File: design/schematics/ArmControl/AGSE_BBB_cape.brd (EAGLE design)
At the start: 71.8 x 54.6 mm, 50 parts, among them Q1 PFET-FQP27P06, Q2 PFET-FQP27P06, Q3 NFET-FQP30N06L, Q4 NFET-FQP30N06L, Q5 PFET-FQP27P06, Q6 PFET-FQP27P06, Q7 NFET-FQP30N06L, Q8 NFET-FQP30N06L, U1 V_REG_LD1085D2

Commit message: updated schematic to move tx/rx connection from UART1 to UART5
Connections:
- net BBB_RX: now also U$1.38; no longer U$1.68, U$1.72
- net BBB_TX: now also U$1.37; no longer U$1.67, U$1.70
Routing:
- net BBB_RX: track 37.2 -> 9.72 mm
- net BBB_TX: track 29.4 -> 23.6 mm
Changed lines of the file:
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@@
 <contactref element="R16" pad="2"/>
 <contactref element="R15" pad="1"/>
-<contactref element="U$1" pad="68"/>
-<contactref element="U$1" pad="72"/>
-<wire x1="38.989" y1="4.699" x2="54.102" y2="19.812" width="0.3048" layer="16"/>
 <wire x1="54.102" y1="19.812" x2="58.293" y2="19.812" width="0.3048" layer="16"/>
 <via x="58.293" y="19.812" extent="1-16" drill="0.6" shape="square"/>
 <wire x1="58.293" y1="19.812" x2="58.293" y2="22.545" width="0.4064" layer="1"/>
 <wire x1="58.293" y1="22.545" x2="61.087" y2="22.545" width="0.4064" layer="1"/>
-<wire x1="38.989" y1="4.699" x2="37.719" y2="5.969" width="0.4064" layer="1"/>
-<wire x1="37.719" y1="5.969" x2="35.433" y2="5.969" width="0.4064" layer="1"/>
-<wire x1="35.433" y1="5.969" x2="34.163" y2="4.699" width="0.4064" layer="1"/>
-<wire x1="34.163" y1="4.699" x2="33.909" y2="4.699" width="0.4064" layer="1"/>
+<contactref element="U$1" pad="38"/>
+<wire x1="58.293" y1="22.545" x2="54.229" y2="52.959" width="0" layer="19" extent="1-1"/>
 </signal>
 <signal name="BBB_TX">
 <contactref element="R14" pad="2"/>
-<contactref element="U$1" pad="67"/>
-<contactref element="U$1" pad="70"/>
-<wire x1="33.909" y1="2.159" x2="36.449" y2="4.699" width="0.4064" layer="1"/>
-<wire x1="36.449" y1="4.699" x2="37.973" y2="6.223" width="0.3048" layer="16"/>
 <wire x1="37.973" y1="6.223" x2="39.497" y2="6.223" width="0.3048" layer="16"/>
 <wire x1="39.497" y1="6.223" x2="51.435" y2="18.161" width="0.3048" layer="16"/>
@@
 <wire x1="51.435" y1="21.209" x2="50.485" y2="20.259" width="0.4064" layer="1"/>
 <wire x1="50.485" y1="20.259" x2="50.485" y2="19.431" width="0.4064" layer="1"/>
+<contactref element="U$1" pad="37"/>
+<wire x1="51.435" y1="21.209" x2="54.229" y2="50.419" width="0" layer="19" extent="1-1"/>
 </signal>
 <signal name="BBB_EQEP2A">

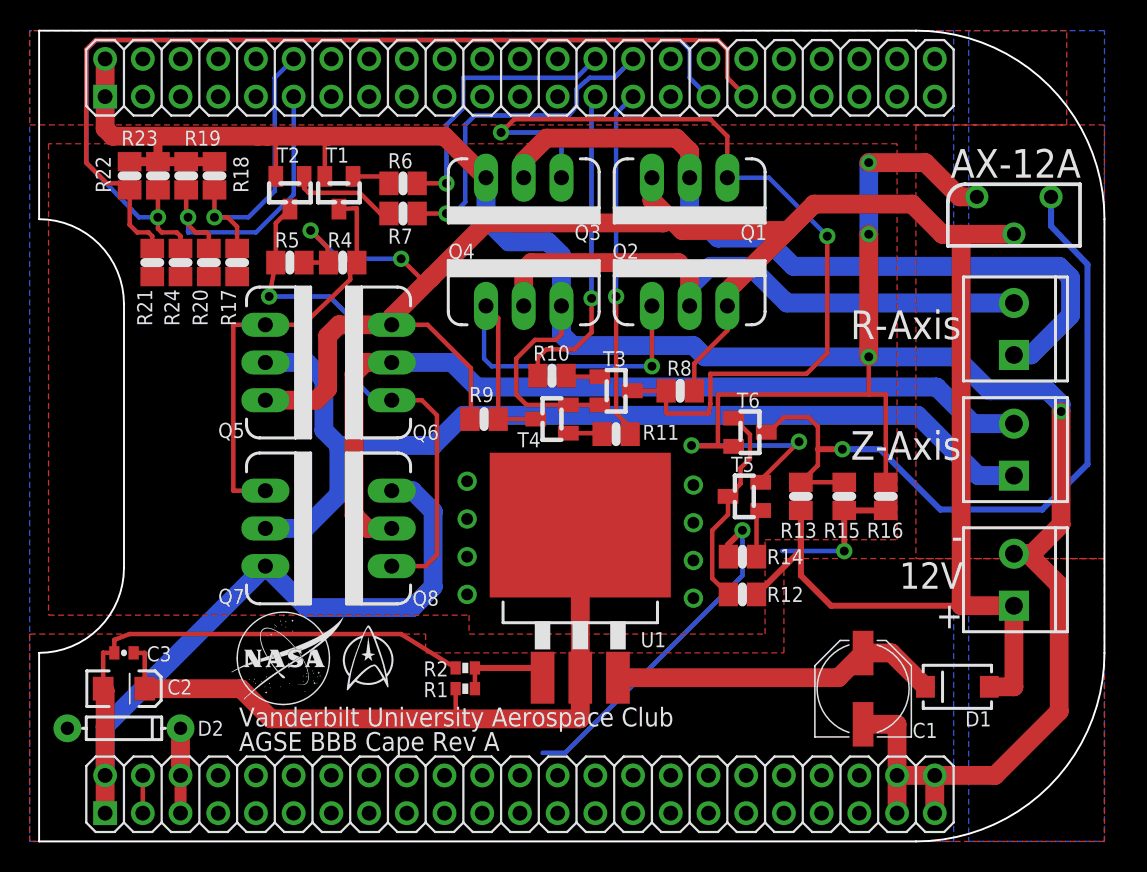
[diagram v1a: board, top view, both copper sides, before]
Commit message: Updated board
* added LEDs for the four motor controls
* moved the serial buffer closer to its new pins (closer to the ax-12a
output)
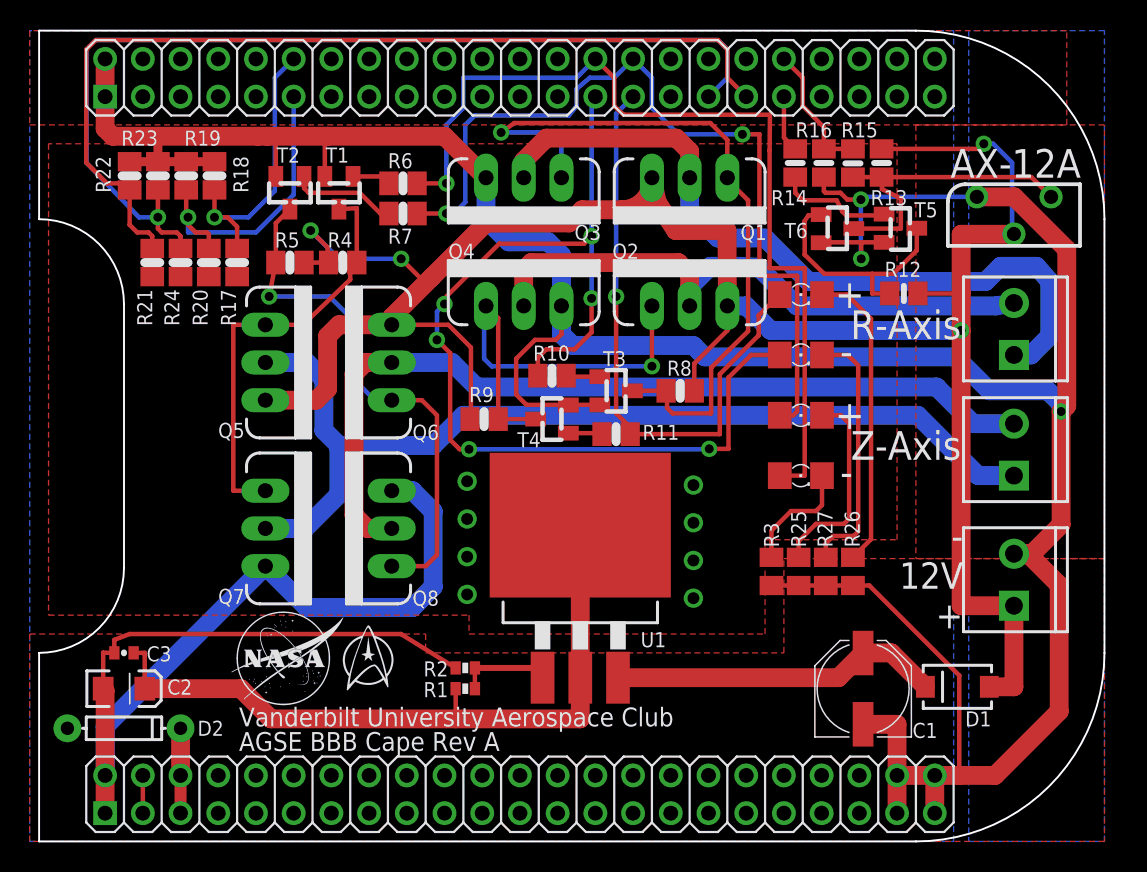
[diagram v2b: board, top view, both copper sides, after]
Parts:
- added D3, D4, D5, D6: (no value), SparkFun-LED:FKIT-LED-1206
- added R25, R26, R27, R3: 50, resistor:M0805
- moved R14 26.8 mm to (55.0, 45.9), turned to 90 degrees
- moved R13 23.1 mm to (60.8, 45.9), turned to 90 degrees
- moved R12 23.0 mm to (62.3, 37.2)
- moved R16 22.8 mm to (56.9, 45.9), turned to 90 degrees
- moved R15 22.5 mm to (58.9, 45.9), turned to 270 degrees
- moved T5 20.9 mm to (62.1, 41.6), turned to 270 degrees
- moved T6 14.9 mm to (57.8, 41.5)
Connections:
- new net N$1: D3.C, R27.2
- new net N$2: D4.C, R26.2
- new net N$5: D5.C, R3.2
- new net N$6: D6.C, R25.2
- net +HEIGHT: now also D6.A
- net +RADIUS: now also D4.A
- net -HEIGHT: now also D5.A
- net -RADIUS: now also D3.A
- net GND: now also R25.1, R26.1, R27.1, R3.1
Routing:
- net -RADIUS: track 21.5 -> 71.2 mm, vias 1 -> 6
- net -HEIGHT: track 19.0 -> 61.7 mm
- net +HEIGHT: track 22.6 -> 56.9 mm, vias 1 -> 2
- net SERVO_TX/RX: track 51.4 -> 21.3 mm, vias 1 -> 0
- net N$2: track 0.00 -> 20.5 mm
- net BBB_TX: track 23.6 -> 3.84 mm, vias 1 -> 0
- net N$1: track 0.00 -> 17.4 mm
- net +RADIUS: track 23.6 -> 40.7 mm
- net N$6: track 0.00 -> 13.6 mm
- net N$13: track 59.4 -> 49.1 mm, vias 2 -> 1
- net N$5: track 0.00 -> 7.89 mm
- net 12V: track 158.8 -> 151.4 mm, vias 2 -> 4
- net N$17: track 3.23 -> 7.87 mm
- net N$18: track 13.8 -> 16.5 mm
- net BBB_EQEP1B: track 64.0 -> 66.6 mm
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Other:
- board text added: "+"
- board text added: "-"

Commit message: Updated board to have molex 4-pin encoder connectors
* also removed unneeded zips
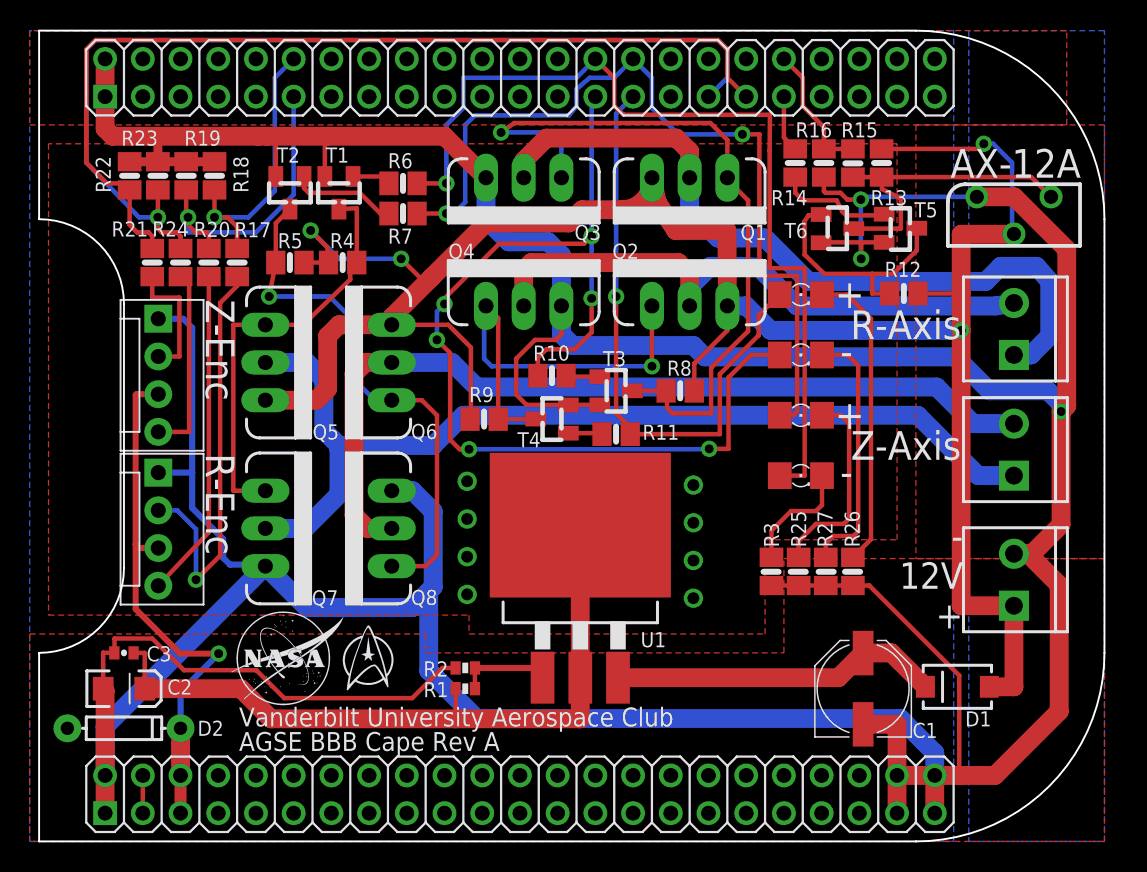
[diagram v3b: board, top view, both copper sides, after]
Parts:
- added RADIAL_ENCODER, VERTICAL_ENCODER: (no value), SparkFun-Connectors:MOLEX-1X4
- moved DRILEGEND 23.9 mm to (0.00, 0.00)
- moved FRAME1 10.7 mm to (0.00, 0.00), turned to 90 degrees
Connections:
- net 5V: now also RADIAL_ENCODER.3, VERTICAL_ENCODER.3
- net GND: now also RADIAL_ENCODER.1, VERTICAL_ENCODER.1
- net RADIAL_ENCODER_A: now also RADIAL_ENCODER.2
- net RADIAL_ENCODER_B: now also RADIAL_ENCODER.4
- net VERTICAL_ENCODER_A: now also VERTICAL_ENCODER.2
- net VERTICAL_ENCODER_B: now also VERTICAL_ENCODER.4
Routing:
- net GND: track 295.0 -> 364.3 mm
- net 5V: track 5.71 -> 36.2 mm, vias 0 -> 1
- net RADIAL_ENCODER_A: track 0.00 -> 28.0 mm, vias 0 -> 1
- net RADIAL_ENCODER_B: track 0.00 -> 22.2 mm
- net VERTICAL_ENCODER_B: track 0.00 -> 13.1 mm
- net VERTICAL_ENCODER_A: track 0.00 -> 8.63 mm
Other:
- board text added: "R-Enc"
- board text added: "Z-Enc"

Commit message: Finalized schematic and board
also added pngs for reference.
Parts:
- moved RADIAL_ENCODER 7.57 mm to (12.1, 17.5), turned to 90 degrees
- moved VERTICAL_ENCODER 7.26 mm to (12.1, 28.2), turned to 90 degrees
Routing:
- net VERTICAL_ENCODER_B: track 13.1 -> 3.11 mm
- net RADIAL_ENCODER_B: track 22.2 -> 14.6 mm
- net RADIAL_ENCODER_A: track 28.0 -> 20.4 mm, vias 1 -> 0
- net GND: track 364.3 -> 358.6 mm
- net 5V: track 36.2 -> 38.1 mm
- net 12V: track 151.4 -> 150.6 mm
- added copper zone on layer 16, net GND
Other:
- board text added: "12V"
- board text removed: "- 12V +"
- board text removed: "- ADD 94V-0 MARKINGS: NO"
- board text removed: "- ADD DATE CODE: NO"
- board text removed: "- ADD UL LOGO: NO"
- board text removed: "- ARRAY: NO"
- board text removed: "- BLIND/BURRIED VIAS: NO"
- board text removed: "- BOARD SIZE: 2.900000 x 2.200000 In."
- board text removed: "- CARBON INK: NO"
- board text removed: "- CLASS 3: NO"
- board text removed: "- CONDUCTIVE FILLED VIAS: NO"
- board text removed: "- CONFORM TO IPC-A-600, CLASS 2: NO"
- board text removed: "- CONTROLLED DIELECTRIC: NO"
- board text removed: "- CONTROLLED IMPEDANCE: NO"
- board text removed: "- COUNTERSINKS/BORES: NO"
- board text removed: "- FINAL THICKNESS: 0.062000"
- board text removed: "- GOLD FINGERS: NO"
- board text removed: "- ITAR COMPLIANT: NO"
- board text removed: "- JUMP SCORING: NO"
- board text removed: "- MASK COLOR: WHITE"
- board text removed: "- MASK PLUGGED VIAS: NO"
- board text removed: "- MASK SIDES: BOTH"
- board text removed: "- MATERIAL: FR-4"
- board text removed: "- MILSPEC: NO"
- board text removed: "- MIN HOLE SIZE: 31"
- board text removed: "- MIN TRACE/SPACE: 10"
- board text removed: "- NO. HOLES UNDER 12 MIL: 0"
- board text removed: "- NO. LAYERS: 2"
- board text removed: "- OUTER CU WEIGHT: 1.000000"
- board text removed: "- PLATED EDGES: NO"
- board text removed: "- PLATED SLOTS: NO"
- board text removed: "- PLATING: Lead Free Solder"
- board text removed: "- RoHS COMPLIANT: YES"
- board text removed: "- SCORING: YES"
- board text removed: "- SILKSCREEN COLOR: BLACK"
- board text removed: "- SILKSCREEN SIDES: FRONT"
- board text removed: "- TAB ROUT: NO"
- board text removed: "- VIA IN PAD: NO"
- board text removed: "- X-OUTS ALLOWED: YES"
- board text removed: "-ALL DIMENSIONS IN INCHES UNESS"
- board text removed: "01-16"
- board text removed: "LAYER-STACK"
- board text removed: "OTHERWISE NOTED"

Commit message: Updated text and positions
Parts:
- moved R12 0.66 mm to (61.6, 37.2)
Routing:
- net N$18: track 16.5 -> 15.4 mm
- net 12V: track 150.6 -> 151.3 mm
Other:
- board text added: "R Axis"
- board text added: "Z Axis"
- board text removed: "R-Axis"
- board text removed: "Z-Axis"
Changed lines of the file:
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@@
 <text x="17.526" y="6.35" size="1.27" layer="21" font="vector">AGSE BBB Cape Rev A</text>
 <text x="66.294" y="18.161" size="1.778" layer="21" font="vector" align="center-right">12V</text>
-<text x="66.167" y="26.924" size="1.9304" layer="21" font="vector" align="center-right">Z-Axis</text>
-<text x="66.167" y="35.052" size="1.9304" layer="21" font="vector" align="center-right">R-Axis</text>
+<text x="66.167" y="26.924" size="1.9304" layer="21" font="vector" align="center-right">Z
+Axis</text>
+<text x="66.167" y="35.052" size="1.9304" layer="21" font="vector" align="center-right">R
+Axis</text>
 <text x="74.2315" y="45.9232" size="1.9304" layer="21" font="vector" align="center-right">AX-12A</text>
 <wire x1="42.291" y1="32.004" x2="43.561" y2="32.004" width="0.3048" layer="21"/>
@@
 <wire x1="47.244" y1="31.115" x2="47.244" y2="30.099" width="0.4064" layer="21"/>
 <wire x1="57.4294" y1="45.9486" x2="56.4134" y2="45.9486" width="0.4064" layer="21"/>
-<wire x1="62.3062" y1="36.6522" x2="62.3062" y2="37.6682" width="0.4064" layer="21"/>
+<wire x1="61.6458" y1="36.6522" x2="61.6458" y2="37.6682" width="0.4064" layer="21"/>
 <wire x1="55.499" y1="45.9486" x2="54.483" y2="45.9486" width="0.4064" layer="21"/>
 <wire x1="60.2996" y1="45.9486" x2="61.3156" y2="45.9486" width="0.4064" layer="21"/>
@@
 <wire x1="57.5818" y1="18.415" x2="56.5658" y2="18.415" width="0.4064" layer="21"/>
 <wire x1="59.3598" y1="18.415" x2="58.3438" y2="18.415" width="0.4064" layer="21"/>
-<text x="16.256" y="26.3906" size="1.9304" layer="21" font="vector" rot="SR270" align="center-left">R-Enc</text>
-<text x="16.256" y="36.7538" size="1.9304" layer="21" font="vector" rot="SR270" align="center-left">Z-Enc</text>
+<text x="14.8336" y="21.2598" size="1.9304" layer="21" font="vector" rot="SR270" align="bottom-center">R-Enc</text>
+<text x="14.8336" y="31.9786" size="1.9304" layer="21" font="vector" rot="SR270" align="bottom-center">Z-Enc</text>
 <text x="73.3552" y="32.0548" size="1.9304" layer="21">+</text>
 <text x="73.7108" y="35.814" size="1.9304" layer="21">-</text>
@@
 <attribute name="VALUE" x="54.6608" y="43.434" size="1.27" layer="27" rot="R270"/>
 </element>
-<element name="R12" library="resistor" package="M0805" value="10K" x="62.3062" y="37.1602" smashed="yes"/>
+<element name="R12" library="resistor" package="M0805" value="10K" x="61.6458" y="37.1602" smashed="yes"/>
 <element name="R13" library="resistor" package="M0805" value="7K" x="60.8076" y="45.9486" smashed="yes" rot="R90"/>
 <element name="R14" library="resistor" package="M0805" value="10K" x="54.991" y="45.9486" smashed="yes" rot="R90"/>
@@
 <wire x1="63.1776" y1="41.5544" x2="63.1776" y2="40.0636" width="0.3048" layer="1"/>
 <wire x1="63.1776" y1="40.0636" x2="61.595" y2="38.481" width="0.3048" layer="1"/>
-<wire x1="61.595" y1="38.481" x2="60.1726" y2="38.481" width="0.3048" layer="1"/>
-<wire x1="60.1726" y1="38.481" x2="56.9468" y2="38.481" width="0.3048" layer="1"/>
+<wire x1="61.595" y1="38.481" x2="60.6044" y2="38.481" width="0.3048" layer="1"/>
+<wire x1="60.6044" y1="38.481" x2="56.9468" y2="38.481" width="0.3048" layer="1"/>
 <wire x1="56.9468" y1="38.481" x2="55.626" y2="39.7764" width="0.3048" layer="1"/>
 <wire x1="55.626" y1="39.7764" x2="55.626" y2="42.037" width="0.3048" layer="1"/>
@@
 <wire x1="55.88" y1="42.418" x2="56.8018" y2="42.418" width="0.3048" layer="1"/>
 <wire x1="56.8018" y1="42.418" x2="56.7358" y2="42.479" width="0.3048" layer="1"/>
-<wire x1="61.3562" y1="37.1602" x2="60.1726" y2="37.1602" width="0.3048" layer="1"/>
-<wire x1="60.1726" y1="37.1602" x2="60.1726" y2="38.481" width="0.3048" layer="1"/>
+<wire x1="60.6958" y1="37.1602" x2="60.6044" y2="37.1602" width="0.3048" layer="1"/>
+<wire x1="60.6044" y1="37.1602" x2="60.6044" y2="38.481" width="0.3048" layer="1"/>
 </signal>
 <signal name="SERVO_TX/RX">
@@
 <wire x1="69.596" y1="41.295" x2="69.723" y2="41.168" width="0.3048" layer="16"/>
 <wire x1="43.307" y1="42.799" x2="45.339" y2="44.958" width="1.27" layer="1" curve="93.471435"/>
-<wire x1="63.2562" y1="37.1602" x2="66.9798" y2="37.1602" width="0.3048" layer="1"/>
+<wire x1="62.5958" y1="37.1602" x2="66.9798" y2="37.1602" width="0.3048" layer="1"/>
 <wire x1="66.9798" y1="39.8272" x2="68.3206" y2="41.168" width="1.27" layer="1"/>
 <wire x1="68.3206" y1="41.168" x2="69.723" y2="41.168" width="1.27" layer="1"/>
@@
 </board>
 </drawing>
+<compatibility>
+<note version="6.3" minversion="6.2.2" severity="warning">
+Since Version 6.2.2 text objects can contain more than one line,
+which will not be processed correctly with this version.
+</note>
+</compatibility>
 </eagle>
